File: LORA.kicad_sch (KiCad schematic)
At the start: 39 parts, among them J5 LoRa_Anten, Q1 BC847, U5 SX1278, U6 MASWSS0192, Y3 32MHz

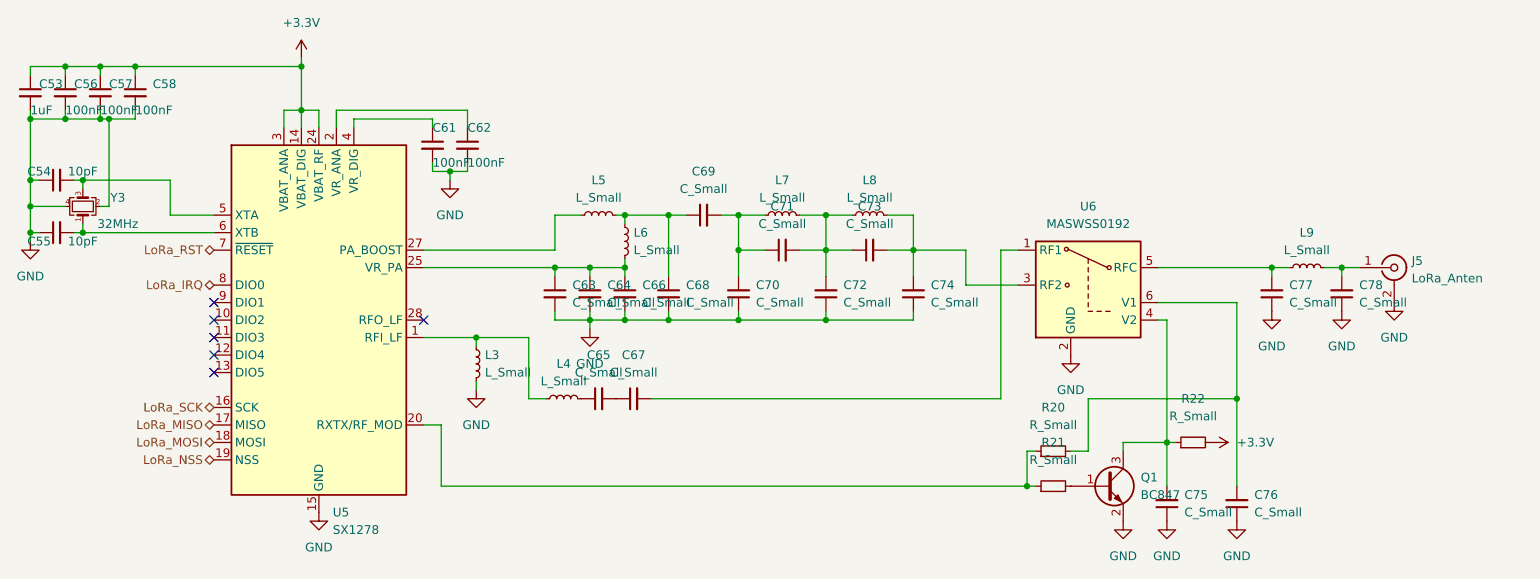
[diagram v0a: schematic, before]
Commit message: Fix USB silkscreen name.
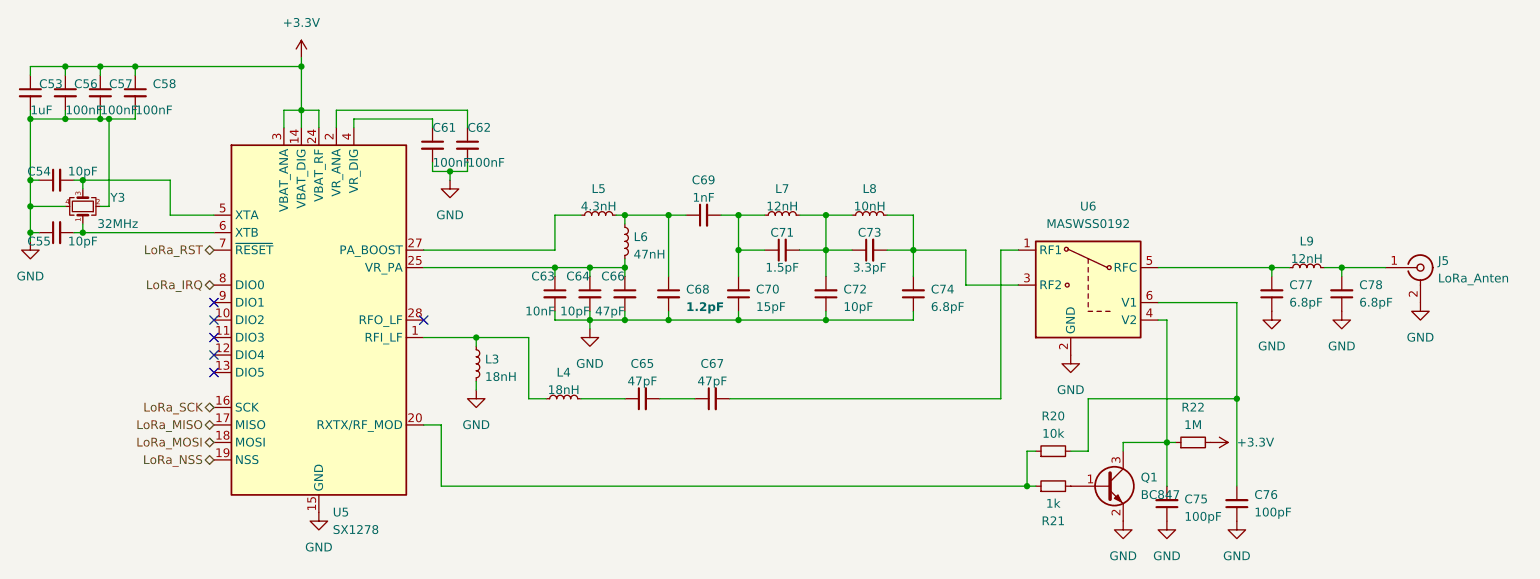
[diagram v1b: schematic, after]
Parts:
- C63: value C_Small -> 10nF
- C64, C72: value C_Small -> 10pF
- C65, C66, C67: value C_Small -> 47pF
- C68: value C_Small -> 1.2pF
- C69: value C_Small -> 1nF
- C70: value C_Small -> 15pF
- C71: value C_Small -> 1.5pF
- C73: value C_Small -> 3.3pF
- C74, C77, C78: value C_Small -> 6.8pF
- C75, C76: value C_Small -> 100pF
- L3, L4: value L_Small -> 18nH
- L5: value L_Small -> 4.3nH
- L6: value L_Small -> 47nH
- L7, L9: value L_Small -> 12nH
- L8: value L_Small -> 10nH
- R20: value R_Small -> 10k
- R21: value R_Small -> 1k
- R22: value R_Small -> 1M
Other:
- moved on the sheet: C65, C67, J5
